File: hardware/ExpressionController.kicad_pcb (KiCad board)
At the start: 2 copper layers, 129 parts, among them Q1 DMP3099L-7, U1 ADP7142AUJZ-3.3, U10 74HC595, U11 SN74LVC126APWR, U12 74HC595, U13 SN74LVC126APWR, U14 74AHCT1G125, U2 ADP7142AUJZ-5.0, U3 ADP7142AUJZ-2.5, U4 AD7718, U5 AD7718, U6 74HC595, U7 SN74LVC126APWR, U8 74HC595, U9 SN74LVC126APWR, Y1 MS1V-T1K-32.768kHz-12.5pF-20P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, Y2 MS1V-T1K-32.768kHz-12.5pF-20P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

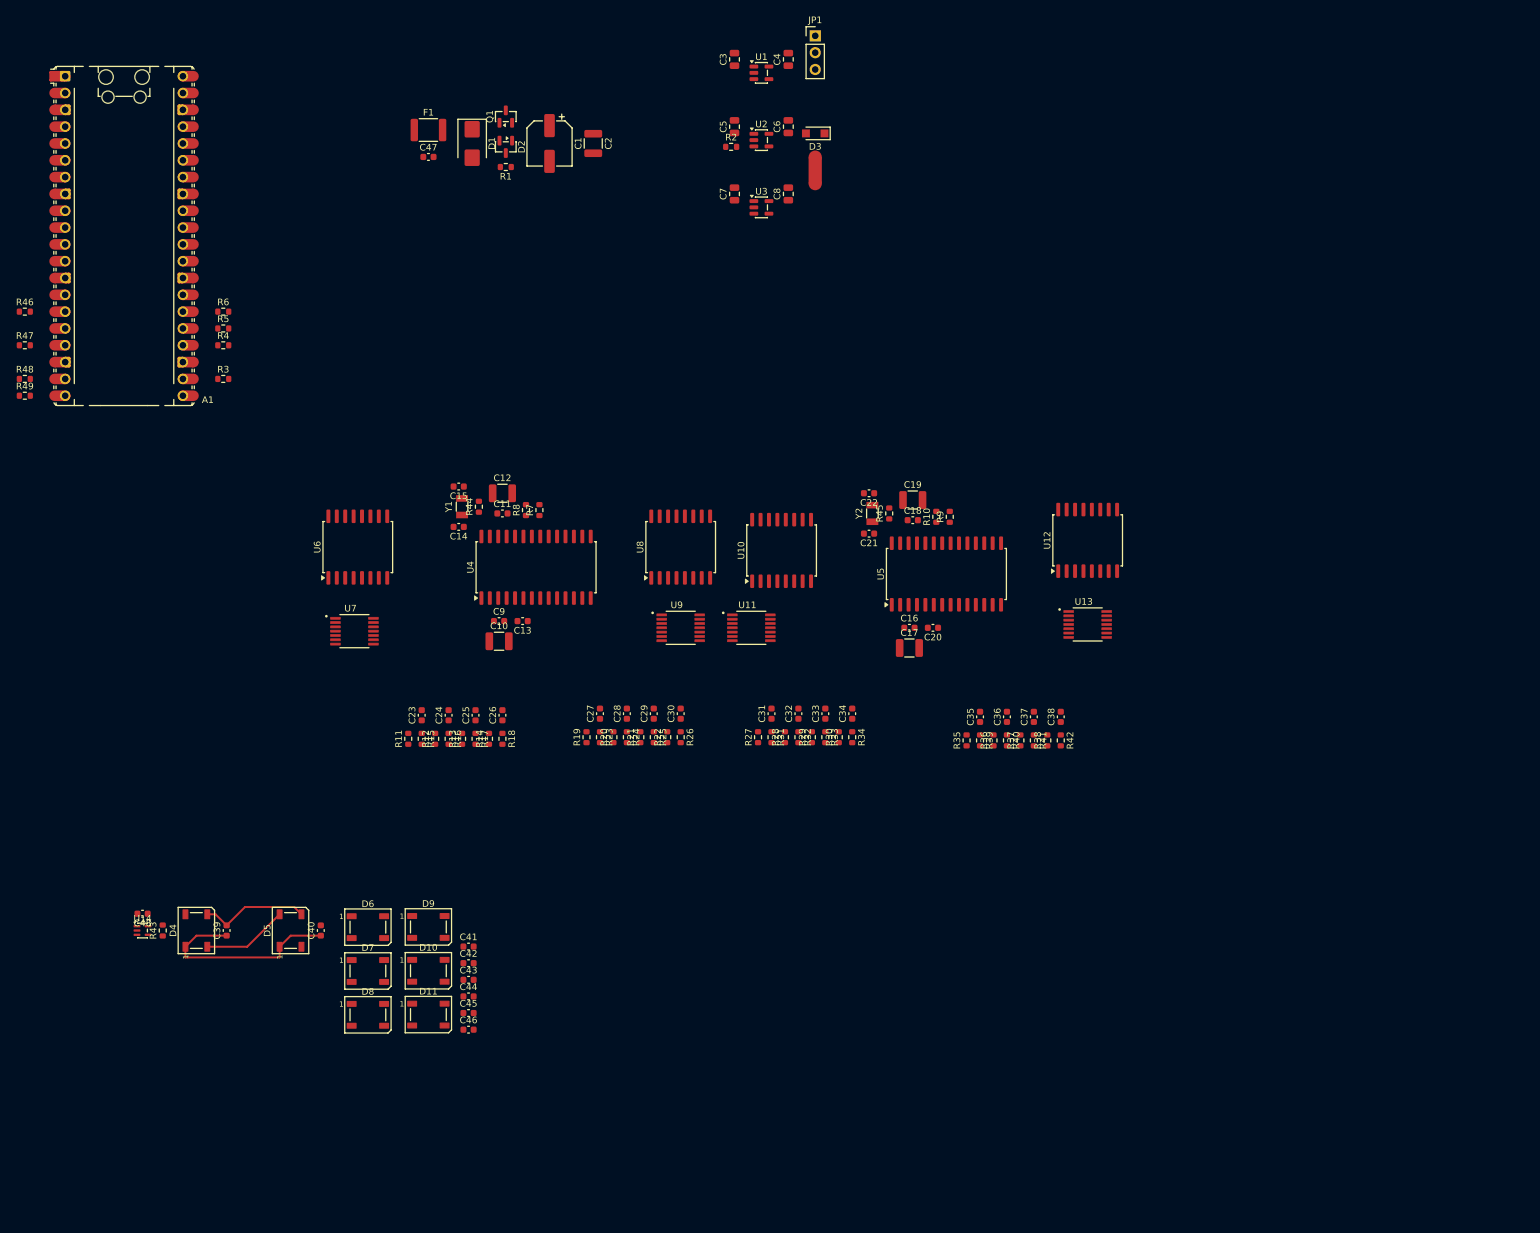
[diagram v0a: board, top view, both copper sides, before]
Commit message: added power consumption measurements and board outline
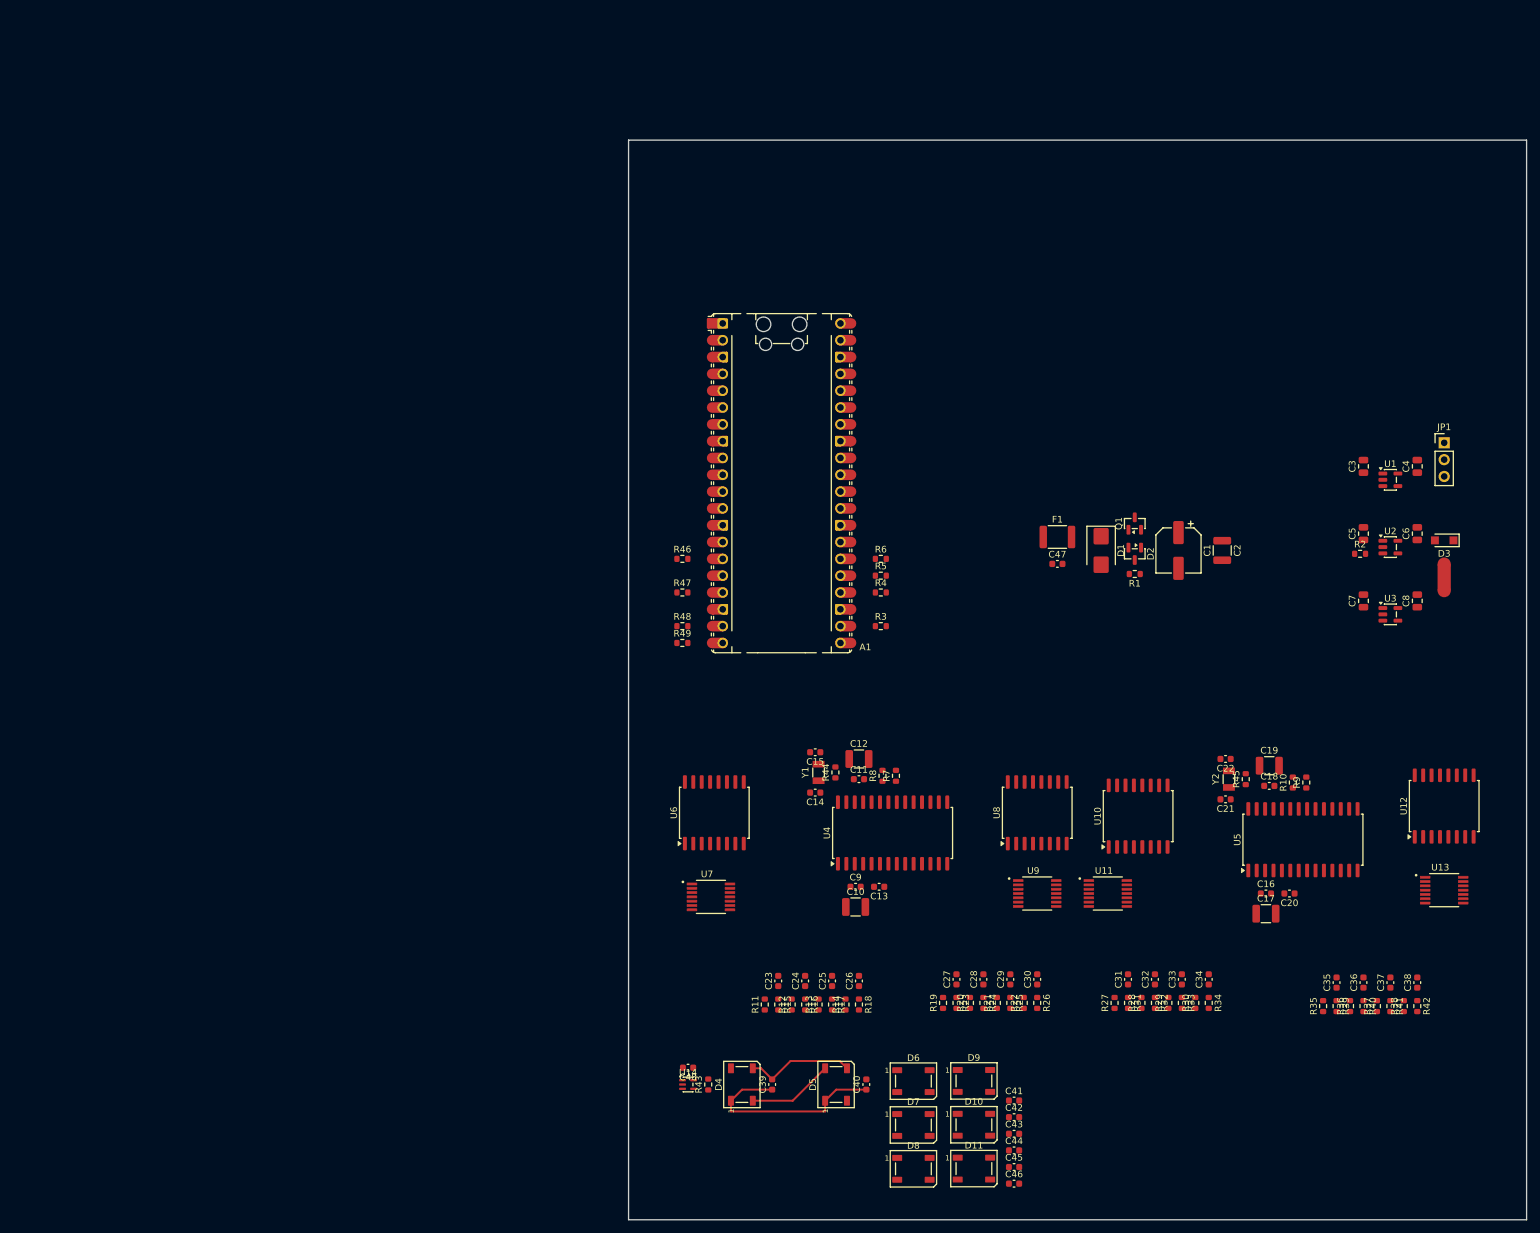
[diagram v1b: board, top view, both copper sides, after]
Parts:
- moved C8 113.1 mm to (248.4, 129.0)
- moved C2 113.1 mm to (218.9, 121.4)
- moved C4 113.1 mm to (248.4, 108.7)
- moved C47 113.1 mm to (194.1, 123.4)
- moved C6 113.1 mm to (248.4, 118.9)
- moved D2 113.1 mm to (205.7, 121.9)
- moved D3 113.1 mm to (252.5, 119.9)
- moved F1 113.1 mm to (194.1, 119.4)
- moved JP1 113.1 mm to (252.5, 105.2)
- moved NT1 113.1 mm to (252.5, 125.5)
- moved Q1 113.1 mm to (205.7, 117.3)
- moved R1 113.1 mm to (205.7, 125.0)
- moved R2 113.1 mm to (239.8, 121.9)
- moved U1 113.1 mm to (244.3, 110.7)
- moved U2 113.1 mm to (244.3, 120.9)
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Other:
- board outline added: 135.6 x 163.1 mm

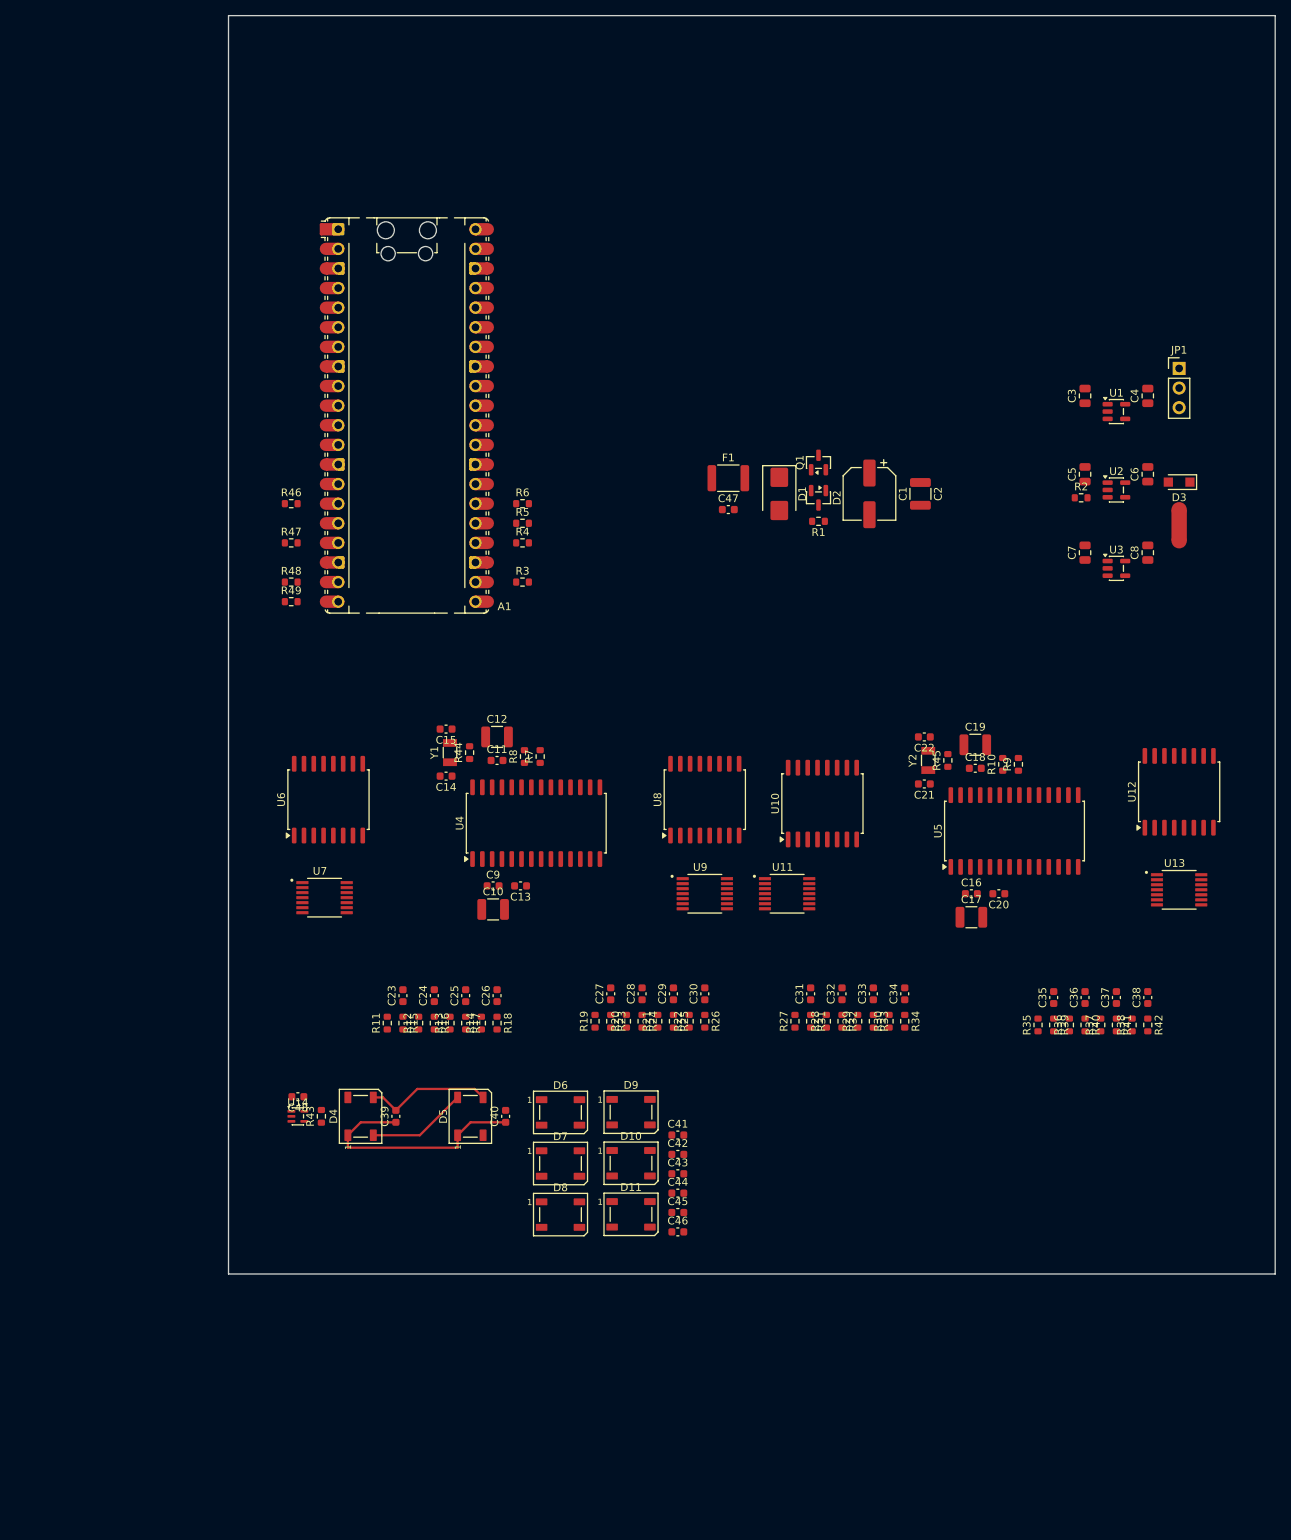
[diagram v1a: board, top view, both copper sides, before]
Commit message: added all footprints, updated to 0805, added layout for Jacks
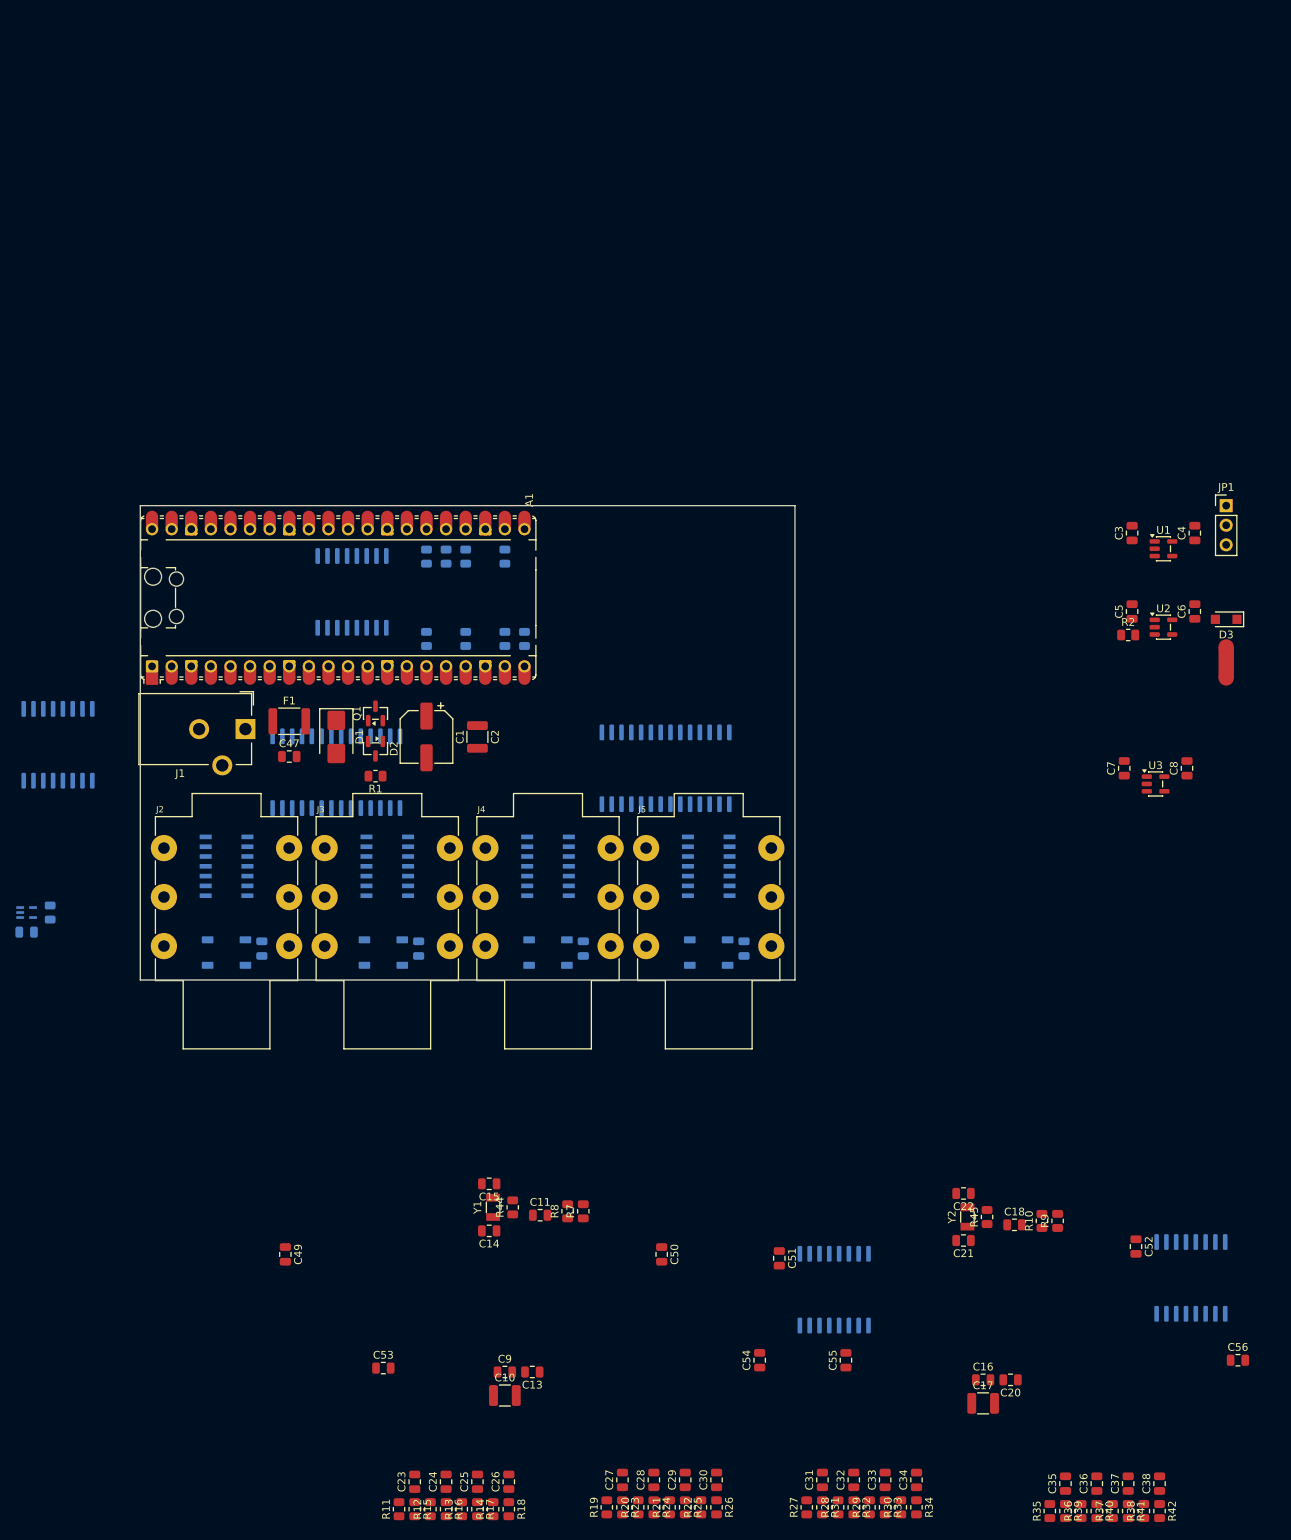
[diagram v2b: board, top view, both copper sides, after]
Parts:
- removed C12, C19: 10u, Capacitor_SMD:C_1210_3225Metric
- removed C43, C44, C45, C46: 100n, Capacitor_SMD:C_0603_1608Metric
- removed D10, D11, D8, D9: WS2812B, LED_SMD:LED_WS2812B_PLCC4_5.0x5.0mm_P3.2mm
- added C49: 100n, Capacitor_SMD:C_0805_2012Metric, F.Cu at (136.7, 220.0)
- added C50: 100n, Capacitor_SMD:C_0805_2012Metric, F.Cu at (185.4, 220.0)
- added C51: 100n, Capacitor_SMD:C_0805_2012Metric, F.Cu at (200.7, 220.5)
- added C52: 100n, Capacitor_SMD:C_0805_2012Metric, F.Cu at (246.9, 218.9)
- added C53: 100n, Capacitor_SMD:C_0805_2012Metric, F.Cu at (149.4, 234.7)
- added C54: 100n, Capacitor_SMD:C_0805_2012Metric, F.Cu at (198.1, 233.7)
- added C55: 100n, Capacitor_SMD:C_0805_2012Metric, F.Cu at (209.3, 233.7)
- added C56: 100n, Capacitor_SMD:C_0805_2012Metric, F.Cu at (260.1, 233.7)
- added J1: DC, Connector_BarrelJack:BarrelJack_CUI_PJ-102AH_Horizontal, F.Cu at (131.5, 151.9)
- added J2: Exp1, Jack_6.35mm_Neutrik_NMJ6HFD4_Horizontal:Jack_6.35mm_Neutrik_NMJ6HFD4_Horizontal, F.Cu at (137.1, 167.3)
- added J3: Exp2, Jack_6.35mm_Neutrik_NMJ6HFD4_Horizontal:Jack_6.35mm_Neutrik_NMJ6HFD4_Horizontal, F.Cu at (158.0, 167.3)
- added J4: Exp3, Jack_6.35mm_Neutrik_NMJ6HFD4_Horizontal:Jack_6.35mm_Neutrik_NMJ6HFD4_Horizontal, F.Cu at (178.8, 167.3)
- added J5: Exp4, Jack_6.35mm_Neutrik_NMJ6HFD4_Horizontal:Jack_6.35mm_Neutrik_NMJ6HFD4_Horizontal, F.Cu at (199.6, 167.3)
- C11, C13, C14, C15, C16, C18, C20, C21, C22, C23, C24, C25, C26, C27, C28, C29, C30, C31, C32, C33, C34, C35, C36, C37, C38, C47, C9: footprint Capacitor_SMD:C_0603_1608Metric -> Capacitor_SMD:C_0805_2012Metric
- C39, C40, C41, C42, C48: footprint Capacitor_SMD:C_0603_1608Metric -> Capacitor_SMD:C_0805_2012Metric; moved to B.Cu
- D4, D5, D6, D7, U10, U12, U14, U4, U5, U6, U8: moved to B.Cu
- R1, R10, R11, R12, R13, R14, R15, R16, R17, R18, R19, R2, R20, R21, R22, R23, R24, R25, R26, R27, R28, R29, R30, R31, R32, R33, R34, R35, R36, R37, R38, R39, R40, R41, R42, R44, R45, R7, R8, R9: footprint Resistor_SMD:R_0603_1608Metric -> Resistor_SMD:R_0805_2012Metric
- R3, R4, R43, R46, R47, R48, R49, R5, R6: footprint Resistor_SMD:R_0603_1608Metric -> Resistor_SMD:R_0805_2012Metric; moved to B.Cu
- U11, U13, U7, U9: value SN74LVC126APWR -> SN74LVC126A; footprint SN74LVC126APWR:SOP65P640X120-14N -> SN74LVC126A:SN74LVC126AD; moved to B.Cu
- moved R1 66.2 mm to (148.3, 158.0)
- moved Q1 66.0 mm to (148.3, 149.9)
- moved D2 66.0 mm to (148.3, 154.4)
- moved C1 65.5 mm to (154.9, 152.9)
- moved C2 65.5 mm to (161.5, 152.9)
- moved D1 65.5 mm to (143.3, 152.9)
- moved C47 65.3 mm to (137.2, 155.4)
- moved F1 65.0 mm to (137.2, 150.9)
- moved C10 63.0 mm to (165.1, 238.3)
- moved C13 63.0 mm to (168.7, 235.2)
- moved C27 63.0 mm to (180.3, 249.2)
- moved C28 63.0 mm to (184.4, 249.2)
- moved C29 63.0 mm to (188.5, 249.2)
- moved C30 63.0 mm to (192.5, 249.2)
- moved C31 63.0 mm to (206.2, 249.2)
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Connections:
- D7 pad 2: Net-(D7-DOUT) -> unconnected-(D7-DOUT-Pad2)
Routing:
- net +5V: track 31.3 -> 0.00 mm
- net GND: track 16.5 -> 0.00 mm
- net Net-(D4-DOUT): track 13.0 -> 0.00 mm
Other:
- board size 135.6 x 163.1 mm -> 84.8 x 61.5 mm

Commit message: more progress in layout
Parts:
- A1: footprint Module:RaspberryPi_Pico_Common_Unspecified -> Pico_2W_with_Header:Pico_2W_with_Header
- R11, R12, R13, R14, R19, R20, R21, R22, R27, R28, R29, R30, R35, R36, R37, R38: moved to B.Cu
- U4, U5: moved to F.Cu
- moved R41 116.6 mm to (195.6, 148.1), turned to 0 degrees
- moved R42 114.8 mm to (195.6, 152.1), turned to 0 degrees
- moved R34 114.4 mm to (172.2, 148.1), turned to 0 degrees
- moved C37 111.5 mm to (195.6, 150.1), turned to 0 degrees
- moved R33 111.0 mm to (167.4, 152.1), turned to 0 degrees
- moved C38 109.9 mm to (195.6, 154.2), turned to 0 degrees
- moved C34 109.3 mm to (172.2, 150.1), turned to 0 degrees
- moved R40 107.5 mm to (195.6, 156.2), turned to 0 degrees
- moved R17 107.3 mm to (138.9, 148.1), turned to 180 degrees
- moved R31 106.2 mm to (172.2, 152.1), turned to 0 degrees
- moved R23 106.2 mm to (162.5, 148.1), turned to 0 degrees
- moved C33 106.0 mm to (167.4, 154.2), turned to 0 degrees
- moved R39 104.3 mm to (199.4, 156.2), turned to 0 degrees
- moved R32 103.8 mm to (172.2, 156.2), turned to 0 degrees
- moved R38 103.3 mm to (186.2, 170.4), turned to -90 degrees
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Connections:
- U11 pad 4: Net-(U10-QD) -> Net-(U10-QC)
- U11 pad 5: Net-(U10-QC) -> Net-(U10-QD)
- U13 pad 4: Net-(U12-QD) -> Net-(U12-QC)
- U13 pad 5: Net-(U12-QC) -> Net-(U12-QD)
- U7 pad 4: Net-(U6-QD) -> Net-(U6-QC)
- U7 pad 5: Net-(U6-QC) -> Net-(U6-QD)
- U9 pad 4: Net-(U8-QD) -> Net-(U8-QC)
- U9 pad 5: Net-(U8-QC) -> Net-(U8-QD)
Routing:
- net Net-(U6-QA): track 0.00 -> 31.5 mm
- net Net-(U6-QE): track 0.00 -> 25.6 mm
- net Net-(U8-QA): track 0.00 -> 25.3 mm
- net Net-(U6-QD): track 0.00 -> 24.3 mm
- net Net-(U6-QC): track 0.00 -> 23.8 mm
- net Net-(U6-QF): track 0.00 -> 23.5 mm
- net Net-(U12-QA): track 0.00 -> 21.1 mm
- net Net-(U10-QA): track 0.00 -> 20.8 mm
- net Net-(U6-QG): track 0.00 -> 20.1 mm
- net Net-(U6-QB): track 0.00 -> 19.1 mm
- net Net-(U8-QE): track 0.00 -> 19.1 mm
- net Net-(U6-QH): track 0.00 -> 19.1 mm
- net Net-(U8-QC): track 0.00 -> 17.9 mm
- net Net-(U8-QD): track 0.00 -> 17.7 mm
- net Net-(U8-QF): track 0.00 -> 17.0 mm
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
